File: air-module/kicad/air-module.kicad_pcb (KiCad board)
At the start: 2 copper layers, 71.1 x 41.1 mm, 38 parts, among them J1 IDC12, J2 ARM_SWD_SMALL, P1 USB_OTG, U1 Alphasense_OPC-N2, U2 nRF52832, U3 Plantower_PM2.5_PMS_5003, U4 TPS2064, U5 BME280, U6 TPS79133

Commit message: Air Geiger Modules PCB update
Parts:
- added G***: LOGO, OPENHARDWARE:OSHWLOGO0.3IN, B.Cu at (133.0, 81.0)

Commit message: Fixes #1
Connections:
- R10 pad 1: MCU-TX -> MCU-RX
- R7 pad 1: MCU-RX -> MCU-TX
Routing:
- net MCU-RX: track 79.1 -> 91.9 mm
- net MCU-TX: track 57.3 -> 65.3 mm, vias 1 -> 3
- net GND: track 233.0 -> 229.8 mm
- net TWI-SCL: track 94.0 -> 95.2 mm

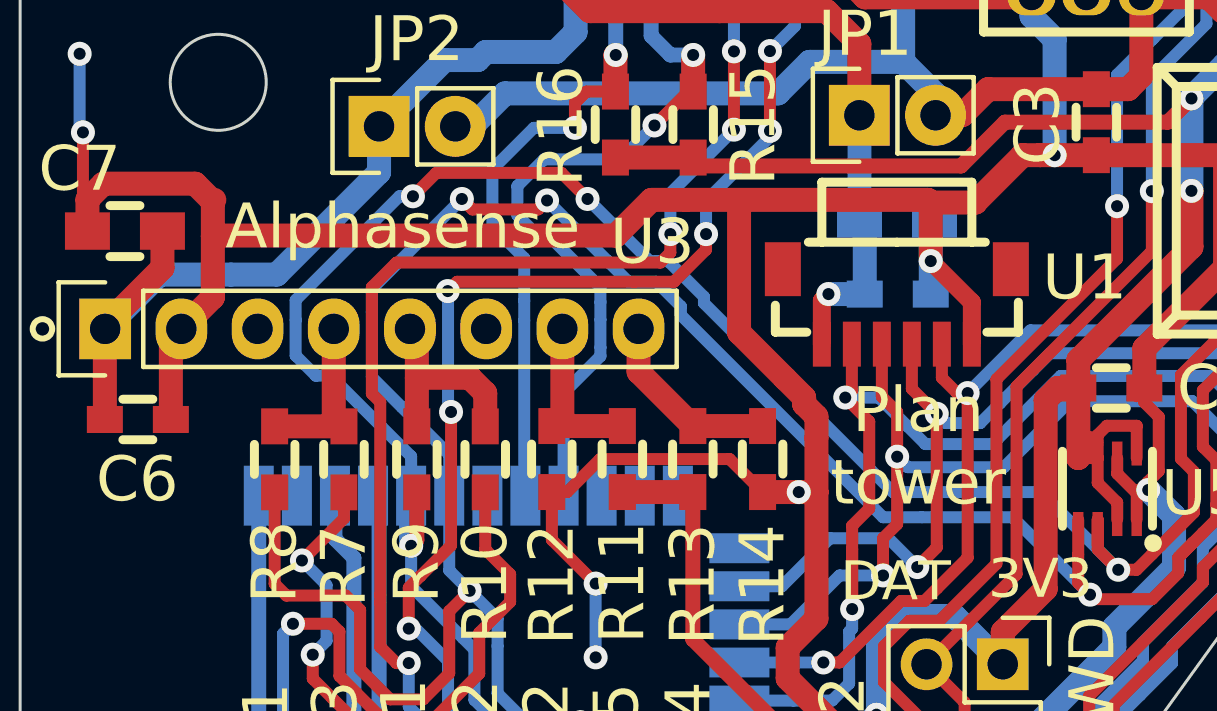
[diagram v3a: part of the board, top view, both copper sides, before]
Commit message: Fixes #9 #8
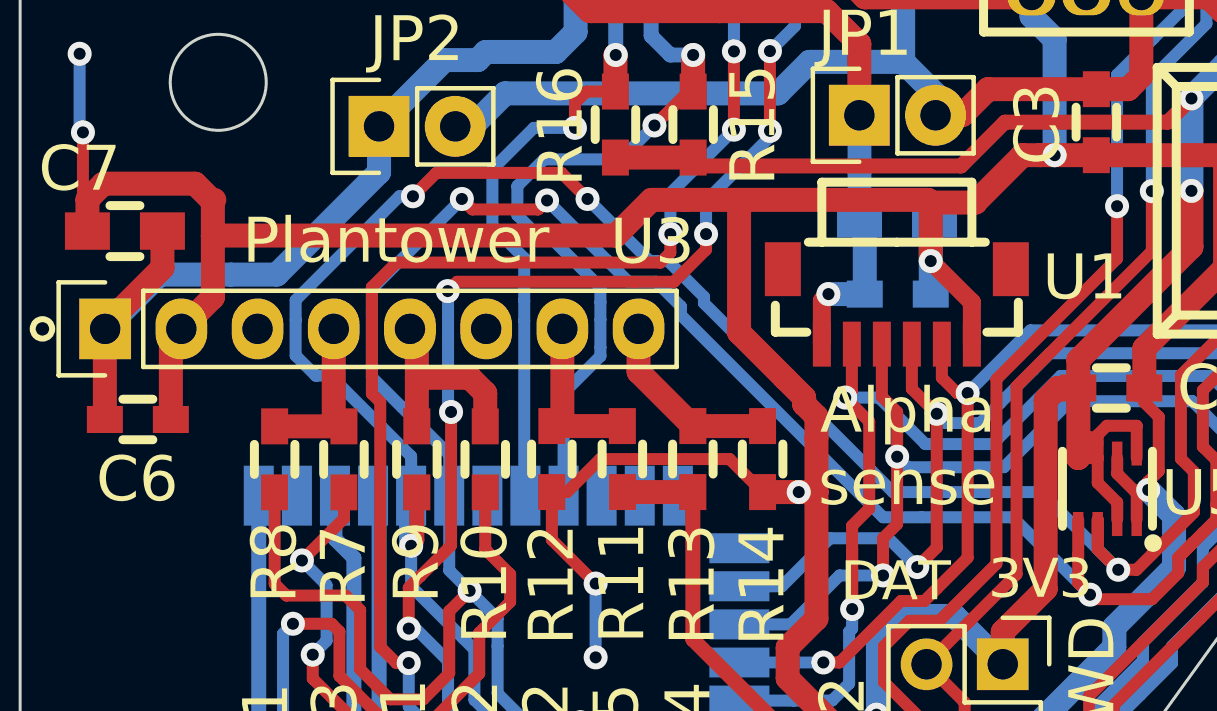
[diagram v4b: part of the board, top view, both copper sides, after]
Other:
- board text added: "Alpha sense"
- board text added: "Plantower"
- board text removed: "Alphasense"
- board text removed: "Plan tower"
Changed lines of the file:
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@@
     (34 B.Paste user)
     (35 F.Paste user)
-    (36 B.SilkS user hide)
-    (37 F.SilkS user hide)
+    (36 B.SilkS user)
+    (37 F.SilkS user)
     (38 B.Mask user)
     (39 F.Mask user)
@@
     (effects (font (size 2 2) (thickness 0.3)) (justify mirror))
   )
-  (gr_text "Plan\ntower" (at 138.275 98.635) (layer F.SilkS)
+  (gr_text Plantower (at 120.86816 91.7825) (layer F.SilkS)
     (effects (font (size 1.5 1.5) (thickness 0.3)))
   )
@@
     (effects (font (size 3 3) (thickness 0.3)) (justify mirror))
   )
-  (gr_text Alphasense (at 121.095 91.305) (layer F.SilkS)
+  (gr_text "Alpha\nsense" (at 137.93188 98.6532) (layer F.SilkS)
     (effects (font (size 1.5 1.5) (thickness 0.3)))
   )

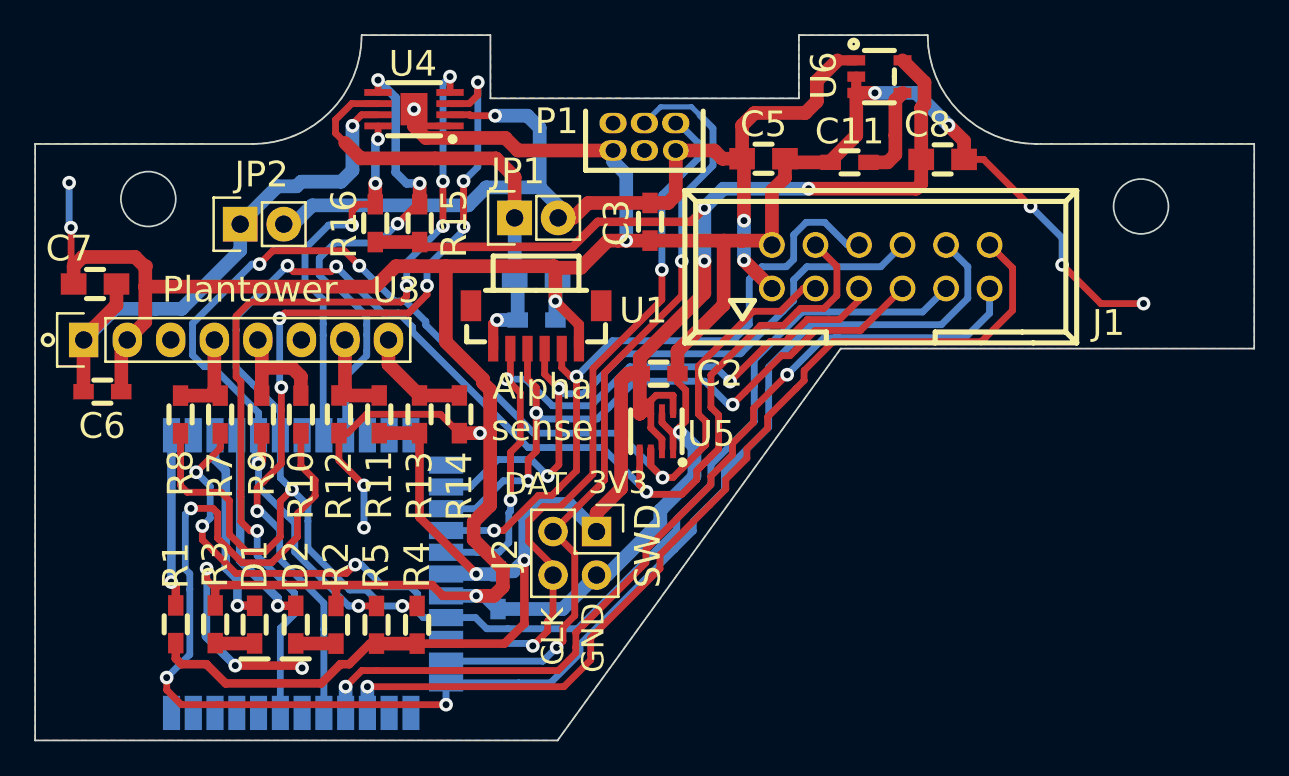
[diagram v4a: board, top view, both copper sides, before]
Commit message: Air Module PCB update, Fixes #4, Fixes #5, Fixes #6, Fixes #7, Fixes #8
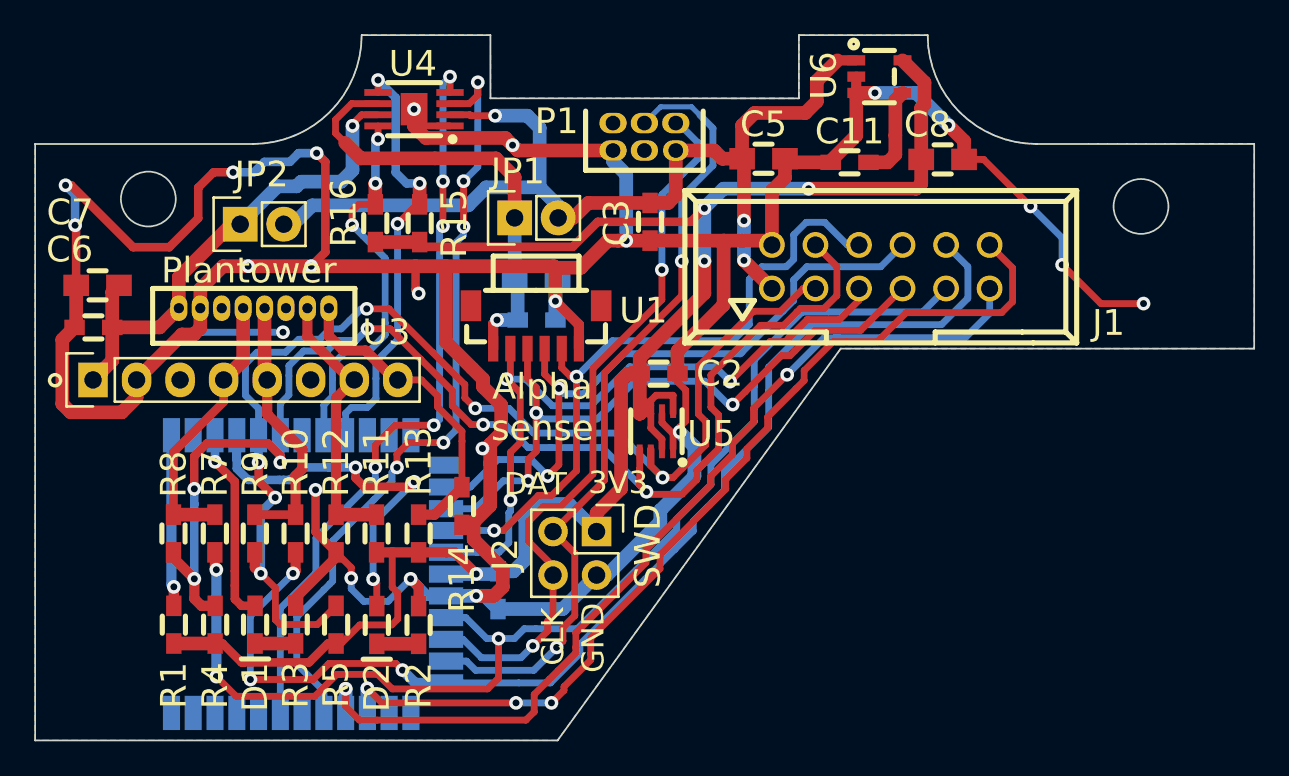
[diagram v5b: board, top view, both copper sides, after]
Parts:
- added P2: CONN_01X08, Molex-53047-0810:Molex-53047-0810, F.Cu at (125.5, 92.9)
- moved R4 11.8 mm to (118.8, 111.3)
- moved R8 6.96 mm to (116.4, 106.0)
- moved R12 6.96 mm to (125.9, 106.0)
- moved R9 6.96 mm to (121.2, 106.0)
- moved R11 6.96 mm to (128.3, 106.0)
- moved R13 6.95 mm to (130.7, 106.0)
- moved R10 6.95 mm to (123.5, 106.0)
- moved R7 6.95 mm to (118.8, 106.0)
- moved R14 5.36 mm to (133.2, 104.4)
- moved R2 4.82 mm to (130.7, 111.3)
- moved D2 4.73 mm to (128.3, 111.3)
- moved R3 4.70 mm to (123.5, 111.3)
- moved C6 3.79 mm to (111.7, 94.0), turned to 180 degrees
- moved U3 2.40 mm to (111.7, 97.0)
- moved R5 2.36 mm to (125.9, 111.3)
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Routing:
- net MCU-RX: track 91.9 -> 67.5 mm
- net TWI-SCL: track 95.2 -> 76.0 mm, vias 5 -> 6
- net +3V3: track 124.2 -> 110.0 mm, vias 5 -> 4
- net GND: track 229.8 -> 243.7 mm, vias 18 -> 23
- net Net-(P2-Pad8): track 6.31 -> 18.7 mm
- net Net-(P2-Pad7): track 5.73 -> 17.7 mm
- net LED-YEL: track 12.0 -> 23.6 mm, vias 1 -> 3
- net Net-(P2-Pad4): track 5.70 -> 16.1 mm
- net Net-(P2-Pad5): track 6.95 -> 15.5 mm
- net EN_ALPHA: track 50.4 -> 43.5 mm
- net TWI-SDA: track 78.5 -> 71.7 mm, vias 5 -> 6
- net EN_PLANT: track 50.8 -> 45.8 mm, vias 7 -> 5
- net MCU-TX: track 65.3 -> 69.9 mm
- net OC_ALPHA: track 28.8 -> 25.3 mm
- net VCC_PLANT: track 32.2 -> 29.5 mm
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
